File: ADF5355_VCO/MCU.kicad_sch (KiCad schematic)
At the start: 37 parts, among them SW2 SW_Push, SW3 SW_DPDT_x2, U2 STM32L433CCTx, Y1 8MHz, Y2 32kHz

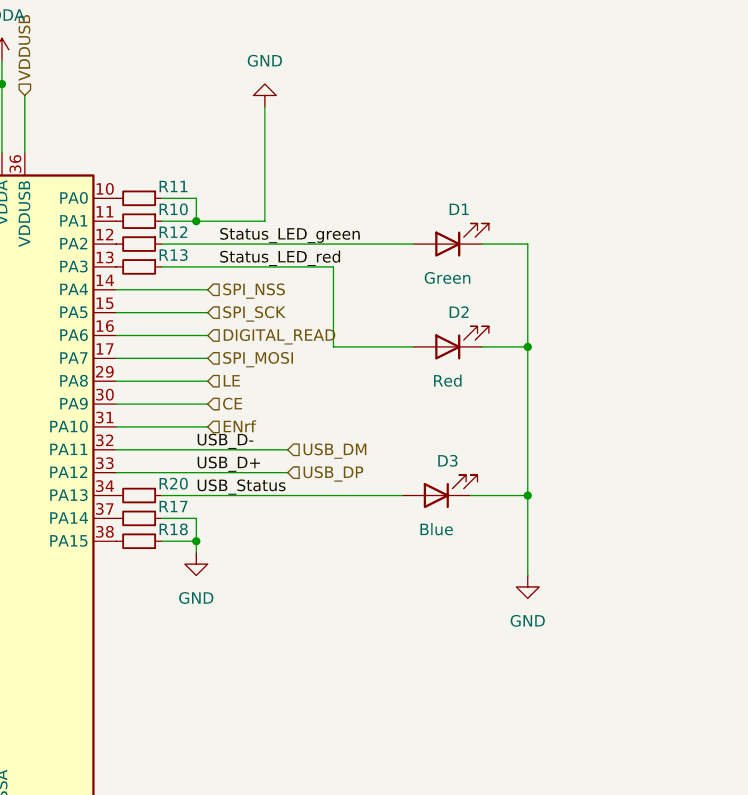
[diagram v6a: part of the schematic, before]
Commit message: Changed the status LED circuit
Changed status LEDs to a BJT driver with 5 V power supply
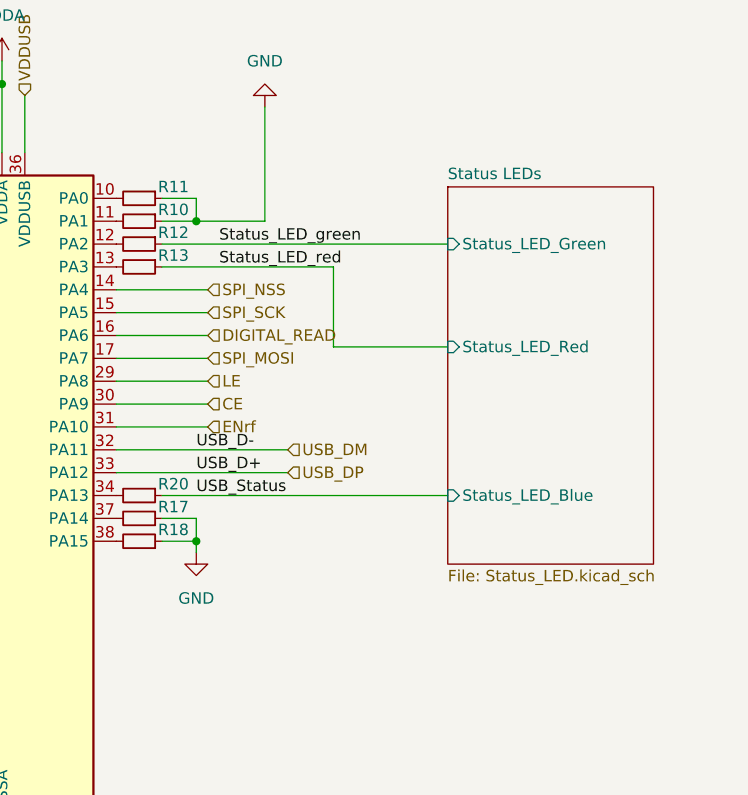
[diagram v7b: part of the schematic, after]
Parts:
- removed D1: Green, symbol Device:LED
- removed D2: Red, symbol Device:LED
- removed D3: Blue, symbol Device:LED
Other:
- added sheet Status LEDs (Status_LED.kicad_sch)
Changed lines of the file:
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@@
   (junction (at 71.12 86.36) (diameter 0) (color 0 0 0 0)
   )
-  (junction (at 180.34 80.01) (diameter 0) (color 0 0 0 0)
-  )
   (junction (at 50.8 165.1) (diameter 0) (color 0 0 0 0)
   )
@@
   (junction (at 143.51 66.04) (diameter 0) (color 0 0 0 0)
   )
-  (junction (at 180.34 96.52) (diameter 0) (color 0 0 0 0)
-  )
   (junction (at 114.3 170.18) (diameter 0) (color 0 0 0 0)
   )
@@
     (stroke (width 0) (type default))
   )
-  (wire (pts (xy 180.34 68.58) (xy 180.34 80.01))
-    (stroke (width 0) (type default))
-  )
   (wire (pts (xy 119.38 57.15) (xy 119.38 58.42))
     (stroke (width 0) (type default))
@@
     (stroke (width 0) (type default))
   )
+  (wire (pts (xy 139.7 96.52) (xy 171.45 96.52))
+    (stroke (width 0) (type default))
+  )
   (bus (pts (xy 87.63 111.76) (xy 87.63 114.3))
     (stroke (width 0) (type default))
@@
     (stroke (width 0) (type default))
   )
-  (wire (pts (xy 173.99 96.52) (xy 180.34 96.52))
-    (stroke (width 0) (type default))
-  )
-  (wire (pts (xy 180.34 96.52) (xy 180.34 105.41))
-    (stroke (width 0) (type default))
-  )
   (wire (pts (xy 116.84 57.15) (xy 116.84 58.42))
     (stroke (width 0) (type default))
@@
     (stroke (width 0) (type default))
   )
-  (wire (pts (xy 175.26 80.01) (xy 180.34 80.01))
-    (stroke (width 0) (type default))
-  )
   (wire (pts (xy 30.48 172.72) (xy 30.48 175.26))
     (stroke (width 0) (type default))
@@
     (stroke (width 0) (type default))
   )
-  (wire (pts (xy 139.7 96.52) (xy 166.37 96.52))
-    (stroke (width 0) (type default))
-  )
   (wire (pts (xy 90.17 93.98) (xy 104.14 93.98))
     (stroke (width 0) (type default))
@@
     (stroke (width 0) (type default))
   )
+  (wire (pts (xy 158.75 80.01) (xy 171.45 80.01))
+    (stroke (width 0) (type default))
+  )
   (wire (pts (xy 24.13 76.2) (xy 29.21 76.2))
     (stroke (width 0) (type default))
@@
     (stroke (width 0) (type default))
   )
-  (wire (pts (xy 175.26 68.58) (xy 180.34 68.58))
-    (stroke (width 0) (type default))
-  )
   (wire (pts (xy 86.36 64.77) (xy 71.12 64.77))
     (stroke (width 0) (type default))
@@
     (stroke (width 0) (type default))
   )
+  (wire (pts (xy 139.7 68.58) (xy 171.45 68.58))
+    (stroke (width 0) (type default))
+  )
   (wire (pts (xy 114.3 162.56) (xy 114.3 160.02))
     (stroke (width 0) (type default))
@@
     (stroke (width 0) (type default))
   )
-  (wire (pts (xy 158.75 80.01) (xy 167.64 80.01))
-    (stroke (width 0) (type default))
-  )
   (wire (pts (xy 90.17 53.34) (xy 90.17 58.42))
     (stroke (width 0) (type default))
@@
     (stroke (width 0) (type default))
   )
-  (wire (pts (xy 139.7 68.58) (xy 167.64 68.58))
-    (stroke (width 0) (type default))
-  )
   (wire (pts (xy 83.82 74.93) (xy 86.36 74.93))
     (stroke (width 0) (type default))
@@
   )
   (wire (pts (xy 90.17 53.34) (xy 90.17 48.26))
-    (stroke (width 0) (type default))
-  )
-  (wire (pts (xy 180.34 80.01) (xy 180.34 96.52))
     (stroke (width 0) (type default))
   )
@@
     (effects (font (size 1.27 1.27)) (justify left))
   )
-  (symbol (lib_id "Device:LED") (at 171.45 68.58 180) (unit 1)
-    (in_bom yes) (on_board yes) (dnp no)
-    (property "Reference" "D1" (at 172.72 64.77 0)
-      (effects (font (size 1.27 1.27)))
-    )
-    (property "Value" "Green" (at 171.45 72.39 0)
-      (effects (font (size 1.27 1.27)))
-    )
-    (property "Footprint" "" (at 171.45 68.58 0)
-      (effects (font (size 1.27 1.27)) hide)
-    )
-    (property "Datasheet" "~" (at 171.45 68.58 0)
-      (effects (font (size 1.27 1.27)) hide)
-    )
-    (pin "1")
-    (pin "2")
-    (instances
-      (project "ADF5355_VCO"
-        (path "/29349b68-071c-451b-9b1e-10b5ef7e12a6/8e6d62a1-615e-4e74-ad33-9284c4715f87"
-          (reference "D1") (unit 1)
-        )
-      )
-    )
-  )
   (symbol (lib_id "Device:C_Small") (at 63.5 64.77 90) (unit 1)
     (in_bom yes) (on_board yes) (dnp no) (fields_autoplaced)
@@
         (path "/29349b68-071c-451b-9b1e-10b5ef7e12a6/8e6d62a1-615e-4e74-ad33-9284c4715f87"
           (reference "C21") (unit 1)
-        )
-      )
-    )
-  )
-  (symbol (lib_id "power:GND") (at 180.34 105.41 0) (unit 1)
-    (in_bom yes) (on_board yes) (dnp no) (fields_autoplaced)
-    (property "Reference" "#PWR030" (at 180.34 111.76 0)
-      (effects (font (size 1.27 1.27)) hide)
-    )
-    (property "Value" "GND" (at 180.34 110.49 0)
-      (effects (font (size 1.27 1.27)))
-    )
-    (property "Footprint" "" (at 180.34 105.41 0)
-      (effects (font (size 1.27 1.27)) hide)
-    )
-    (property "Datasheet" "" (at 180.34 105.41 0)
-      (effects (font (size 1.27 1.27)) hide)
-    )
-    (pin "1")
-    (instances
-      (project "ADF5355_VCO"
-        (path "/29349b68-071c-451b-9b1e-10b5ef7e12a6/8e6d62a1-615e-4e74-ad33-9284c4715f87"
-          (reference "#PWR030") (unit 1)
         )
       )
@@
     )
   )
-  (symbol (lib_id "Device:LED") (at 171.45 80.01 180) (unit 1)
-    (in_bom yes) (on_board yes) (dnp no)
-    (property "Reference" "D2" (at 172.72 76.2 0)
-      (effects (font (size 1.27 1.27)))
-    )
-    (property "Value" "Red" (at 171.45 83.82 0)
-      (effects (font (size 1.27 1.27)))
-    )
-    (property "Footprint" "" (at 171.45 80.01 0)
-      (effects (font (size 1.27 1.27)) hide)
-    )
-    (property "Datasheet" "~" (at 171.45 80.01 0)
-      (effects (font (size 1.27 1.27)) hide)
-    )
-    (pin "1")
-    (pin "2")
-    (instances
-      (project "ADF5355_VCO"
-        (path "/29349b68-071c-451b-9b1e-10b5ef7e12a6/8e6d62a1-615e-4e74-ad33-9284c4715f87"
-          (reference "D2") (unit 1)
-        )
-      )
-    )
-  )
   (symbol (lib_id "power:GND") (at 114.3 172.72 0) (unit 1)
     (in_bom yes) (on_board yes) (dnp no) (fields_autoplaced)
@@
         (path "/29349b68-071c-451b-9b1e-10b5ef7e12a6/8e6d62a1-615e-4e74-ad33-9284c4715f87"
           (reference "#PWR041") (unit 1)
-        )
-      )
-    )
-  )
-  (symbol (lib_id "Device:LED") (at 170.18 96.52 180) (unit 1)
-    (in_bom yes) (on_board yes) (dnp no)
-    (property "Reference" "D3" (at 171.45 92.71 0)
-      (effects (font (size 1.27 1.27)))
-    )
-    (property "Value" "Blue" (at 170.18 100.33 0)
-      (effects (font (size 1.27 1.27)))
-    )
-    (property "Footprint" "" (at 170.18 96.52 0)
-      (effects (font (size 1.27 1.27)) hide)
-    )
-    (property "Datasheet" "~" (at 170.18 96.52 0)
-      (effects (font (size 1.27 1.27)) hide)
-    )
-    (pin "1")
-    (pin "2")
-    (instances
-      (project "ADF5355_VCO"
-        (path "/29349b68-071c-451b-9b1e-10b5ef7e12a6/8e6d62a1-615e-4e74-ad33-9284c4715f87"
-          (reference "D3") (unit 1)
         )
       )
@@
       )
     )
+  )
+  (sheet (at 171.45 62.23) (size 22.86 41.91) (fields_autoplaced)
+    (stroke (width 0.1524) (type solid))
+    (fill (color 255 240 101 1.0000))
+    (property "Sheetname" "Status LEDs" (at 171.45 61.5184 0)
+      (effects (font (size 1.27 1.27)) (justify left bottom))
+    )
+    (property "Sheetfile" "Status_LED.kicad_sch" (at 171.45 104.7246 0)
+      (effects (font (size 1.27 1.27)) (justify left top))
+    )
+    (pin "Status_LED_Green" input (at 171.45 68.58 180)
+      (effects (font (size 1.27 1.27)) (justify left))
+    )
+    (pin "Status_LED_Red" input (at 171.45 80.01 180)
+      (effects (font (size 1.27 1.27)) (justify left))
+    )
+    (pin "Status_LED_Blue" input (at 171.45 96.52 180)
+      (effects (font (size 1.27 1.27)) (justify left))
+    )
+    (instances
+      (project "ADF5355_VCO"
+        (path "/29349b68-071c-451b-9b1e-10b5ef7e12a6/8e6d62a1-615e-4e74-ad33-9284c4715f87" (page "8"))
+      )
+    )
